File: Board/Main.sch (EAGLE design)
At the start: 7 parts, among them M1 LB1909MC, M2 LB1909MC

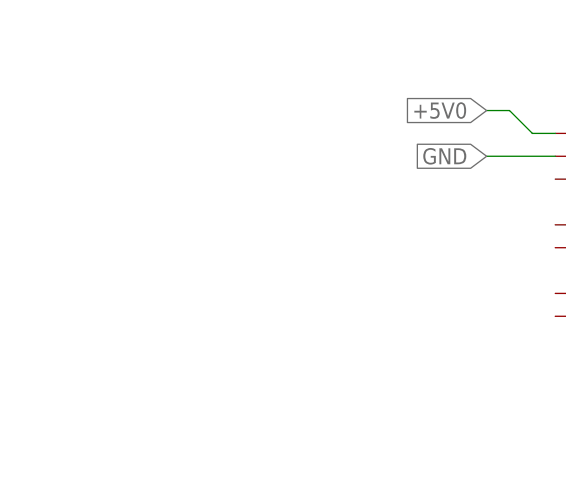
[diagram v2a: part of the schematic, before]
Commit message: Add USB connector
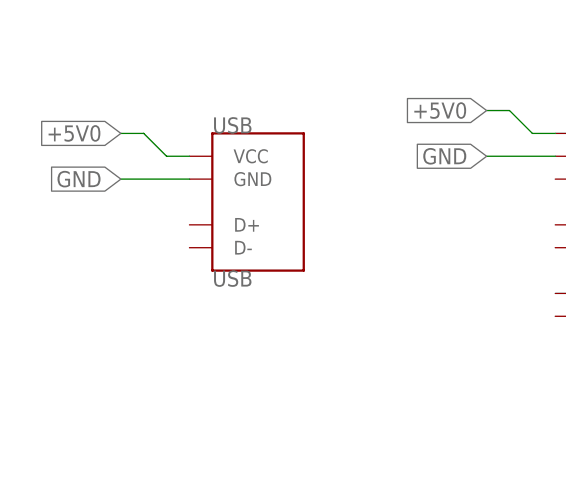
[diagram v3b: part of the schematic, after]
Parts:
- added USB: USB, Components:USB
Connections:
- net +5V0: now also USB.VCC
- net GND: now also USB.GND
- net N$2: now also U$4.B2; no longer U$4.P$2
- net N$3: now also U$3.B2; no longer U$3.P$2
- net N$4: now also U$3.B1; no longer U$3.P$1
- net N$5: now also U$4.B1; no longer U$4.P$1
- net N$6: now also U$4.A1; no longer U$4.P$3
- net N$7: now also U$4.A2; no longer U$4.P$4
- net N$8: now also U$3.A1; no longer U$3.P$3
- net N$9: now also U$3.A2; no longer U$3.P$4
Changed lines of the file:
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@@
 <setting verticaltext="up"/>
 </settings>
-<grid distance="0.1" unitdist="inch" unit="inch" style="lines" multiple="1" display="yes" altdistance="0.01" altunitdist="inch" altunit="inch"/>
+<grid distance="0.1" unitdist="inch" unit="inch" style="lines" multiple="1" display="no" altdistance="0.01" altunitdist="inch" altunit="inch"/>
 <layers>
 <layer number="1" name="Top" color="4" fill="1" visible="no" active="no"/>
@@
 <part name="U$3" library="Components" deviceset="MOTOR" device=""/>
 <part name="U$4" library="Components" deviceset="MOTOR" device=""/>
+<part name="USB" library="Components" deviceset="USB" device=""/>
 </parts>
 <sheets>
@@
 <instance part="U$3" gate="G$1" x="157.48" y="43.18" smashed="yes"/>
 <instance part="U$4" gate="G$1" x="157.48" y="68.58" smashed="yes"/>
+<instance part="USB" gate="G$1" x="7.62" y="109.22" smashed="yes">
+<attribute name="NAME" x="2.54" y="116.84" size="1.778" layer="95" font="vector"/>
+<attribute name="VALUE" x="2.54" y="101.6" size="1.778" layer="96" font="vector" align="top-left"/>
+</instance>
 </instances>
 <busses>
@@
 <label x="111.76" y="53.34" size="1.778" layer="95" rot="R180" xref="yes"/>
 </segment>
+<segment>
+<pinref part="USB" gate="G$1" pin="GND"/>
+<wire x1="0" y1="111.76" x2="-7.62" y2="111.76" width="0.1524" layer="91"/>
+<label x="-7.62" y="111.76" size="1.778" layer="95" rot="R180" xref="yes"/>
+</segment>
 </net>
 <net name="+3V3" class="0">
@@
 <wire x1="35.56" y1="119.38" x2="33.02" y2="119.38" width="0.1524" layer="91"/>
 <label x="33.02" y="119.38" size="1.778" layer="95" rot="R180" xref="yes"/>
+</segment>
+<segment>
+<pinref part="USB" gate="G$1" pin="VCC"/>
+<wire x1="0" y1="114.3" x2="-2.54" y2="114.3" width="0.1524" layer="91"/>
+<wire x1="-2.54" y1="114.3" x2="-5.08" y2="116.84" width="0.1524" layer="91"/>
+<wire x1="-5.08" y1="116.84" x2="-7.62" y2="116.84" width="0.1524" layer="91"/>
+<label x="-7.62" y="116.84" size="1.778" layer="95" rot="R180" xref="yes"/>
 </segment>
 </net>
@@
 <wire x1="144.78" y1="68.58" x2="147.32" y2="68.58" width="0.1524" layer="91"/>
 <wire x1="147.32" y1="68.58" x2="149.86" y2="66.04" width="0.1524" layer="91"/>
-<pinref part="U$4" gate="G$1" pin="P$2"/>
+<pinref part="U$4" gate="G$1" pin="B2"/>
 </segment>
 </net>
@@
 <wire x1="144.78" y1="43.18" x2="147.32" y2="43.18" width="0.1524" layer="91"/>
 <wire x1="147.32" y1="43.18" x2="149.86" y2="40.64" width="0.1524" layer="91"/>
-<pinref part="U$3" gate="G$1" pin="P$2"/>
+<pinref part="U$3" gate="G$1" pin="B2"/>
 </segment>
 </net>
@@
 <segment>
 <pinref part="M2" gate="G$1" pin="OUT3"/>
-<pinref part="U$3" gate="G$1" pin="P$1"/>
+<pinref part="U$3" gate="G$1" pin="B1"/>
 <wire x1="144.78" y1="45.72" x2="149.86" y2="45.72" width="0.1524" layer="91"/>
 </segment>
@@
 <segment>
 <pinref part="M1" gate="G$1" pin="OUT3"/>
-<pinref part="U$4" gate="G$1" pin="P$1"/>
+<pinref part="U$4" gate="G$1" pin="B1"/>
 <wire x1="144.78" y1="71.12" x2="149.86" y2="71.12" width="0.1524" layer="91"/>
 </segment>
@@
 <net name="N$6" class="0">
 <segment>
-<pinref part="U$4" gate="G$1" pin="P$3"/>
+<pinref part="U$4" gate="G$1" pin="A1"/>
 <wire x1="154.94" y1="76.2" x2="152.4" y2="78.74" width="0.1524" layer="91"/>
 <pinref part="M1" gate="G$1" pin="OUT2"/>
@@
 <wire x1="144.78" y1="81.28" x2="157.48" y2="81.28" width="0.1524" layer="91"/>
 <wire x1="157.48" y1="81.28" x2="160.02" y2="78.74" width="0.1524" layer="91"/>
-<pinref part="U$4" gate="G$1" pin="P$4"/>
+<pinref part="U$4" gate="G$1" pin="A2"/>
 <wire x1="160.02" y1="78.74" x2="160.02" y2="76.2" width="0.1524" layer="91"/>
 </segment>
@@
 <pinref part="M2" gate="G$1" pin="OUT2"/>
 <wire x1="144.78" y1="53.34" x2="152.4" y2="53.34" width="0.1524" layer="91"/>
-<pinref part="U$3" gate="G$1" pin="P$3"/>
+<pinref part="U$3" gate="G$1" pin="A1"/>
 <wire x1="152.4" y1="53.34" x2="154.94" y2="50.8" width="0.1524" layer="91"/>
 </segment>
@@
 <wire x1="144.78" y1="55.88" x2="157.48" y2="55.88" width="0.1524" layer="91"/>
 <wire x1="157.48" y1="55.88" x2="160.02" y2="53.34" width="0.1524" layer="91"/>
-<pinref part="U$3" gate="G$1" pin="P$4"/>
+<pinref part="U$3" gate="G$1" pin="A2"/>
 <wire x1="160.02" y1="53.34" x2="160.02" y2="50.8" width="0.1524" layer="91"/>
 </segment>
